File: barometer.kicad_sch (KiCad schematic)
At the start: 0 parts

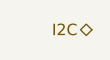
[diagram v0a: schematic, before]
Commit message: Fixed bus names
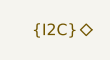
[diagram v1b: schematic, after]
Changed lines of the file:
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@@
     (title "Phoenix Barometer")
   )
-  (hierarchical_label "I2C" (shape bidirectional) (at 26.67 25.4 180)
+  (hierarchical_label "{I2C}" (shape bidirectional) (at 26.67 25.4 180)
     (effects (font (size 1.27 1.27)) (justify right))
   )

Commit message: Various updates because I forgot to commit for a while
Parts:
- added C16: 100nF, symbol Device:C
- added U5: MS5637-02BA03, symbol Sensor:MS5637-02BA03
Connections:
- new net +3.3V: C16.1, U5. (VDD)
- new net GND: C16.2, U5. (VDD)
- new net SCL: U5. (VDD)
- new net SDA: U5. (VDD)
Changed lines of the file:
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@@
     (title "Phoenix Barometer")
   )
-  (hierarchical_label "{I2C}" (shape bidirectional) (at 26.67 25.4 180)
-    (effects (font (size 1.27 1.27)) (justify right))
+  (junction (at 106.68 76.2) (diameter 0) (color 0 0 0 0)
+  )
+  (junction (at 106.68 87.63) (diameter 0) (color 0 0 0 0)
+  )
+  (bus_entry (at 151.13 85.09) (size -2.54 2.54)
+    (stroke (width 0) (type default) (color 0 0 0 0))
+  )
+  (bus_entry (at 151.13 73.66) (size -2.54 2.54)
+    (stroke (width 0) (type default) (color 0 0 0 0))
+  )
+  (wire (pts (xy 142.24 76.2) (xy 148.59 76.2))
+    (stroke (width 0) (type default) (color 0 0 0 0))
+  )
+  (wire (pts (xy 115.57 87.63) (xy 106.68 87.63))
+    (stroke (width 0) (type default) (color 0 0 0 0))
+  )
+  (wire (pts (xy 106.68 87.63) (xy 106.68 93.98))
+    (stroke (width 0) (type default) (color 0 0 0 0))
+  )
+  (bus (pts (xy 151.13 73.66) (xy 151.13 85.09))
+    (stroke (width 0) (type default) (color 0 0 0 0))
+  )
+  (wire (pts (xy 142.24 87.63) (xy 148.59 87.63))
+    (stroke (width 0) (type default) (color 0 0 0 0))
+  )
+  (bus (pts (xy 151.13 71.12) (xy 151.13 73.66))
+    (stroke (width 0) (type default) (color 0 0 0 0))
+  )
+  (wire (pts (xy 115.57 76.2) (xy 106.68 76.2))
+    (stroke (width 0) (type default) (color 0 0 0 0))
+  )
+  (wire (pts (xy 106.68 85.09) (xy 106.68 87.63))
+    (stroke (width 0) (type default) (color 0 0 0 0))
+  )
+  (wire (pts (xy 106.68 76.2) (xy 106.68 77.47))
+    (stroke (width 0) (type default) (color 0 0 0 0))
+  )
+  (wire (pts (xy 106.68 76.2) (xy 106.68 68.58))
+    (stroke (width 0) (type default) (color 0 0 0 0))
+  )
+  (label "SCL" (at 143.51 76.2 0)
+    (effects (font (size 1.27 1.27)) (justify left bottom))
+  )
+  (label "I2C write address: 0x6C" (at 140.97 99.06 0)
+    (effects (font (size 1.27 1.27)) (justify left bottom))
+  )
+  (label "SDA" (at 143.51 87.63 0)
+    (effects (font (size 1.27 1.27)) (justify left bottom))
+  )
+  (label "I2C Read Address: 0x6D" (at 140.97 95.25 0)
+    (effects (font (size 1.27 1.27)) (justify left bottom))
+  )
+  (hierarchical_label "{I2C}" (shape bidirectional) (at 151.13 71.12 90)
+    (effects (font (size 1.27 1.27)) (justify left))
+  )
+  (symbol (lib_id "Sensor:MS5637-02BA03") (at 127 69.85 0) (unit 1)
+    (in_bom yes) (on_board yes)
+    (property "Reference" "U5" (id 0) (at 129.54 78.74 0))
+    (property "Value" "MS5637-02BA03" (id 1) (at 129.54 81.28 0))
+    (property "Footprint" "" (id 2) (at 127 69.85 0)
+      (effects (font (size 1.27 1.27)) hide)
+    )
+    (property "Datasheet" "" (id 3) (at 127 69.85 0)
+      (effects (font (size 1.27 1.27)) hide)
+    )
+    (pin "")
+    (pin "")
+    (pin "")
+    (pin "")
+  )
+  (symbol (lib_id "Device:C") (at 106.68 81.28 0) (unit 1)
+    (in_bom yes) (on_board yes) (fields_autoplaced)
+    (property "Reference" "C16" (id 0) (at 110.49 80.0099 0)
+      (effects (font (size 1.27 1.27)) (justify left))
+    )
+    (property "Value" "100nF" (id 1) (at 110.49 82.5499 0)
+      (effects (font (size 1.27 1.27)) (justify left))
+    )
+    (property "Footprint" "" (id 2) (at 107.6452 85.09 0)
+      (effects (font (size 1.27 1.27)) hide)
+    )
+    (property "Datasheet" "~" (id 3) (at 106.68 81.28 0)
+      (effects (font (size 1.27 1.27)) hide)
+    )
+    (pin "1")
+    (pin "2")
+  )
+  (symbol (lib_id "power:+3.3V") (at 106.68 68.58 0) (unit 1)
+    (in_bom yes) (on_board yes) (fields_autoplaced)
+    (property "Reference" "#PWR032" (id 0) (at 106.68 72.39 0)
+      (effects (font (size 1.27 1.27)) hide)
+    )
+    (property "Value" "+3.3V" (id 1) (at 106.68 63.5 0))
+    (property "Footprint" "" (id 2) (at 106.68 68.58 0)
+      (effects (font (size 1.27 1.27)) hide)
+    )
+    (property "Datasheet" "" (id 3) (at 106.68 68.58 0)
+      (effects (font (size 1.27 1.27)) hide)
+    )
+    (pin "1")
+  )
+  (symbol (lib_id "power:GND") (at 106.68 93.98 0) (unit 1)
+    (in_bom yes) (on_board yes) (fields_autoplaced)
+    (property "Reference" "#PWR033" (id 0) (at 106.68 100.33 0)
+      (effects (font (size 1.27 1.27)) hide)
+    )
+    (property "Value" "GND" (id 1) (at 106.68 99.06 0))
+    (property "Footprint" "" (id 2) (at 106.68 93.98 0)
+      (effects (font (size 1.27 1.27)) hide)
+    )
+    (property "Datasheet" "" (id 3) (at 106.68 93.98 0)
+      (effects (font (size 1.27 1.27)) hide)
+    )
+    (pin "1")
   )
 )

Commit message: Added footprint
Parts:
- U5: footprint (none) -> YAR_Sensors:MS5637_1
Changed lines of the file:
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@@
     (property "Reference" "U5" (id 0) (at 129.54 78.74 0))
     (property "Value" "MS5637-02BA03" (id 1) (at 129.54 81.28 0))
-    (property "Footprint" "" (id 2) (at 127 69.85 0)
+    (property "Footprint" "YAR_Sensors:MS5637_1" (id 2) (at 127 69.85 0)
       (effects (font (size 1.27 1.27)) hide)
     )

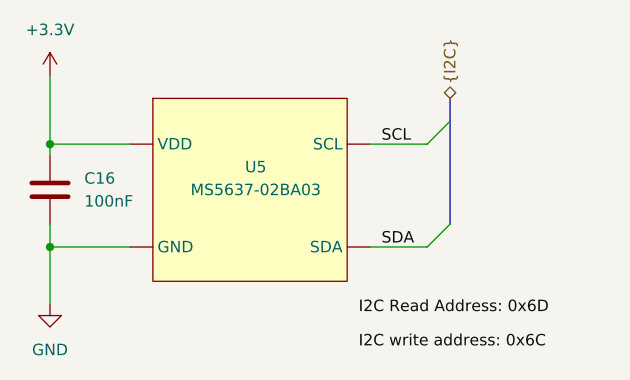
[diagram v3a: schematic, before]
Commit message: Connected the sensors, flash chip, Need to connect the radio and GPS
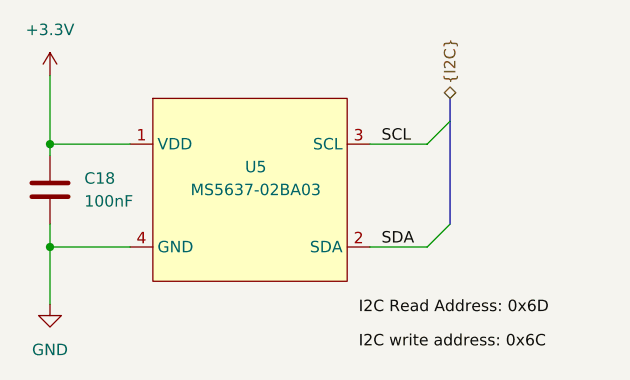
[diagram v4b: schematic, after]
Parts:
- C18: renamed from C16; footprint (none) -> Capacitor_SMD:C_0603_1608Metric
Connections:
- net +3.3V: now also U5.1 (VDD); no longer U5. (VDD)
- net GND: now also U5.4 (GND); no longer U5. (VDD)
- net SCL: now also U5.3 (SCL); no longer U5. (VDD)
- net SDA: now also U5.2 (SDA); no longer U5. (VDD)
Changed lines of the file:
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@@
       (effects (font (size 1.27 1.27)) hide)
     )
-    (pin "")
-    (pin "")
-    (pin "")
-    (pin "")
+    (pin "1")
+    (pin "2")
+    (pin "3")
+    (pin "4")
   )
   (symbol (lib_id "Device:C") (at 106.68 81.28 0) (unit 1)
     (in_bom yes) (on_board yes) (fields_autoplaced)
-    (property "Reference" "C16" (id 0) (at 110.49 80.0099 0)
+    (property "Reference" "C18" (id 0) (at 110.49 80.0099 0)
       (effects (font (size 1.27 1.27)) (justify left))
     )
@@
       (effects (font (size 1.27 1.27)) (justify left))
     )
-    (property "Footprint" "" (id 2) (at 107.6452 85.09 0)
+    (property "Footprint" "Capacitor_SMD:C_0603_1608Metric" (id 2) (at 107.6452 85.09 0)
       (effects (font (size 1.27 1.27)) hide)
     )
@@
   (symbol (lib_id "power:+3.3V") (at 106.68 68.58 0) (unit 1)
     (in_bom yes) (on_board yes) (fields_autoplaced)
-    (property "Reference" "#PWR032" (id 0) (at 106.68 72.39 0)
+    (property "Reference" "#PWR034" (id 0) (at 106.68 72.39 0)
       (effects (font (size 1.27 1.27)) hide)
     )
@@
   (symbol (lib_id "power:GND") (at 106.68 93.98 0) (unit 1)
     (in_bom yes) (on_board yes) (fields_autoplaced)
-    (property "Reference" "#PWR033" (id 0) (at 106.68 100.33 0)
+    (property "Reference" "#PWR035" (id 0) (at 106.68 100.33 0)
       (effects (font (size 1.27 1.27)) hide)
     )

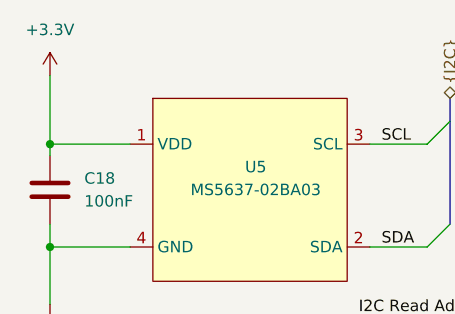
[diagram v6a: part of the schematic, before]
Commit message: Fixed power ports
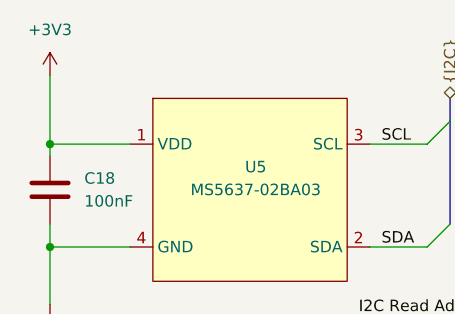
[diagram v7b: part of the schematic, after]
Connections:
- net +3.3V renamed +3V3
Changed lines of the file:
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@@
     (effects (font (size 1.27 1.27)) (justify left))
+  )
+  (symbol (lib_id "power:+3V3") (at 106.68 68.58 0) (unit 1)
+    (in_bom yes) (on_board yes) (fields_autoplaced)
+    (property "Reference" "#PWR0103" (id 0) (at 106.68 72.39 0)
+      (effects (font (size 1.27 1.27)) hide)
+    )
+    (property "Value" "+3V3" (id 1) (at 106.68 63.5 0))
+    (property "Footprint" "" (id 2) (at 106.68 68.58 0)
+      (effects (font (size 1.27 1.27)) hide)
+    )
+    (property "Datasheet" "" (id 3) (at 106.68 68.58 0)
+      (effects (font (size 1.27 1.27)) hide)
+    )
+    (pin "1")
   )
   (symbol (lib_id "Sensor:MS5637-02BA03") (at 127 69.85 0) (unit 1)
@@
     (pin "2")
   )
-  (symbol (lib_id "power:+3.3V") (at 106.68 68.58 0) (unit 1)
-    (in_bom yes) (on_board yes) (fields_autoplaced)
-    (property "Reference" "#PWR032" (id 0) (at 106.68 72.39 0)
-      (effects (font (size 1.27 1.27)) hide)
-    )
-    (property "Value" "+3.3V" (id 1) (at 106.68 63.5 0))
-    (property "Footprint" "" (id 2) (at 106.68 68.58 0)
-      (effects (font (size 1.27 1.27)) hide)
-    )
-    (property "Datasheet" "" (id 3) (at 106.68 68.58 0)
-      (effects (font (size 1.27 1.27)) hide)
-    )
-    (pin "1")
-  )
   (symbol (lib_id "power:GND") (at 106.68 93.98 0) (unit 1)
